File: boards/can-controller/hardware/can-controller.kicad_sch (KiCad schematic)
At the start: 1 part, among them J1 RPi_GPIO

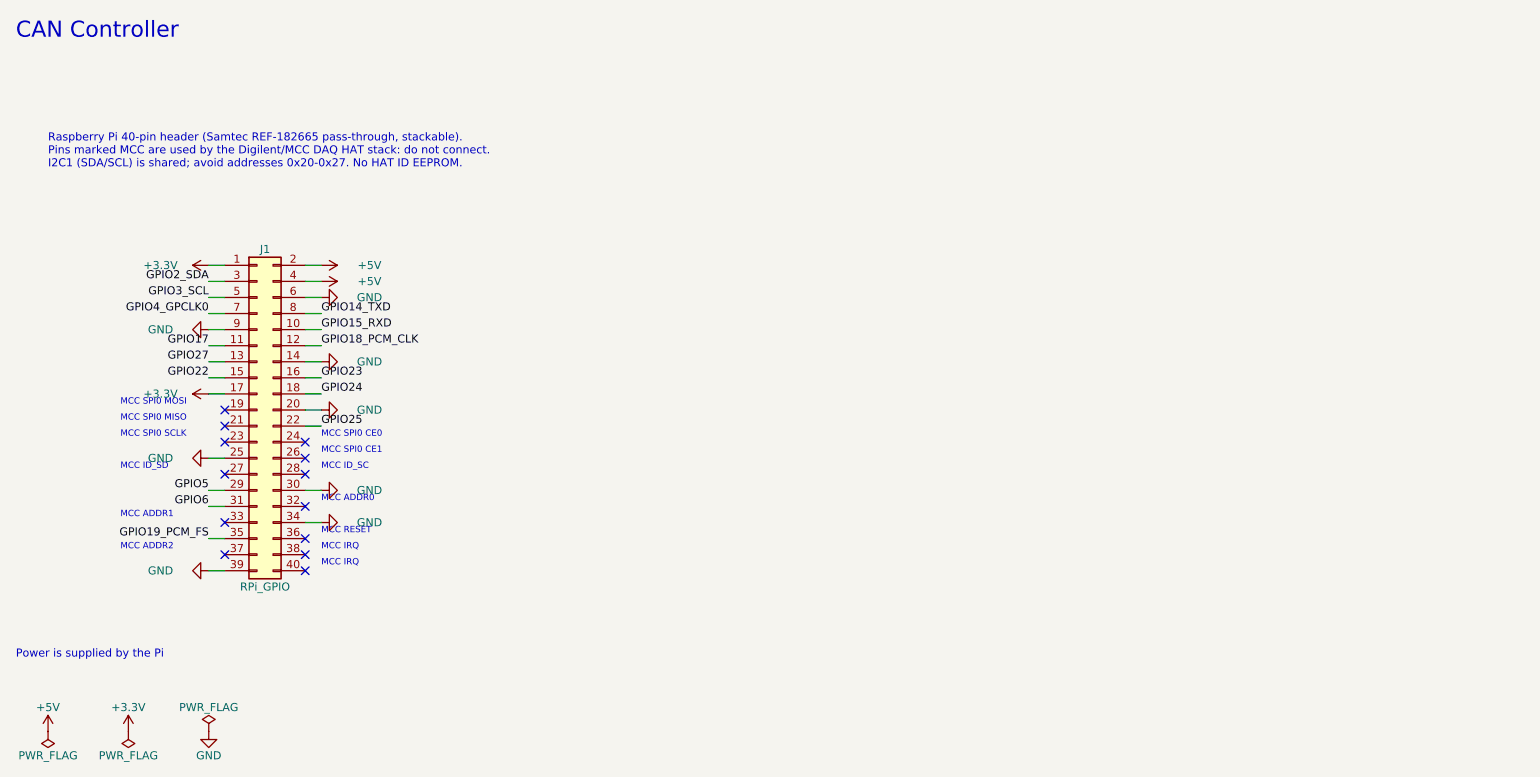
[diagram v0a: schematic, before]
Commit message: can-controller: first schematic capture (7 sheets), footprints parked
- gen_schematic.py (first capture only, like can-ssr's): MCU/USB/power,
  CAN x4 (ISO1044BD; +12 V fuse fitted on CAN1, DNP on CAN2-4), 12 V input
  (NANO2 fuse, SUD50P04-08 reverse-polarity P-FET, SMBJ15A, R-78E 5 V for
  the bus sides, TLP293 12 V status), relay drive (2 x ISO6740, ULN2803A,
  logic-side LEDs), GPIO (8 x 4.7k + BAT54S), analog in (MCP3428, dividers
  referenced to VMID because the ADC cannot go below VSS), analog out
  (MCP4922 + LM4040 2.5 V, LM358B gain 4 on a 13 V TPS61040 boost,
  470R + 15 V Zener output protection)
- MCU pin map checked against the PPS group tables of DS60001519E
- ERC 0, parity clean; only isolators span the two domains
- PCB: footprints synced and parked; template copper removed
- sync_pcb.py now carries the DNP attribute to the PCB
- House DRC rule: 0.15 mm annular ring for the GCT USB4085 only
- 3D models for SOIC-4 (SOP-4) and the 1812 PTC (C_1812 stand-in)

Co-Authored-By: Claude Opus 5.5 <noreply@anthropic.com>
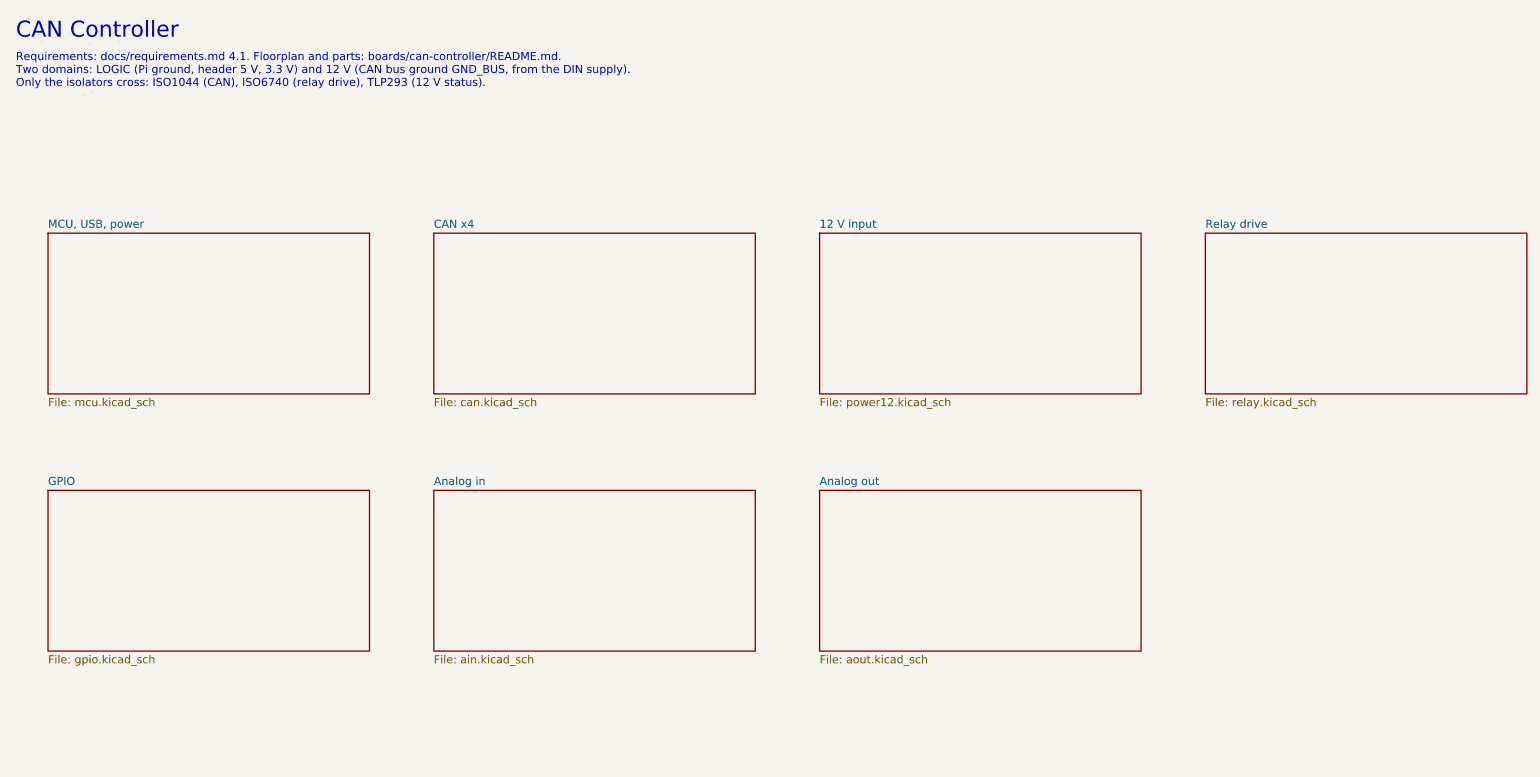
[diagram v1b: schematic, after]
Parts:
- removed J1: RPi_GPIO, Thl_Connector:Samtec_REF-182665_2x20_P2.54mm_PassThrough, symbol Connector_Generic:Conn_02x20_Odd_Even
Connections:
- no-connect marks 13 -> 0
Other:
- added sheet 12 V input (power12.kicad_sch)
- added sheet Analog in (ain.kicad_sch)
- added sheet Analog out (aout.kicad_sch)
- added sheet CAN x4 (can.kicad_sch)
- added sheet GPIO (gpio.kicad_sch)
- added sheet MCU, USB, power (mcu.kicad_sch)
- added sheet Relay drive (relay.kicad_sch)
- note added: "Requirements: docs/requirements.md 4.1. Floorplan and parts: boards/can-controller/README.md. Two domains: LOGIC (Pi ground, header 5 V, 3.3 V) and 12 V (CAN bus ground GND_BUS, from the DIN supply). Only the isolators cross: ISO1044 (CAN), ISO6740 (relay drive), TLP293 (12 V status)."
- note removed: "MCC ADDR0"
- note removed: "MCC ADDR1"
- note removed: "MCC ADDR2"
- note removed: "MCC ID_SC"
- note removed: "MCC ID_SD"
- note removed: "MCC IRQ"
- note removed: "MCC RESET"
- note removed: "MCC SPI0 CE0"
- note removed: "MCC SPI0 CE1"
- note removed: "MCC SPI0 MISO"
- note removed: "MCC SPI0 MOSI"
- note removed: "MCC SPI0 SCLK"
- note removed: "Power is supplied by the Pi"
- note removed: "Raspberry Pi 40-pin header (Samtec REF-182665 pass-through, stackable). Pins marked MCC are used by the Digilent/MCC DAQ HAT stack: do not connect. I2C1 (SDA/SCL) is shared; avoid addresses 0x20-0x27. No HAT ID EEPROM."

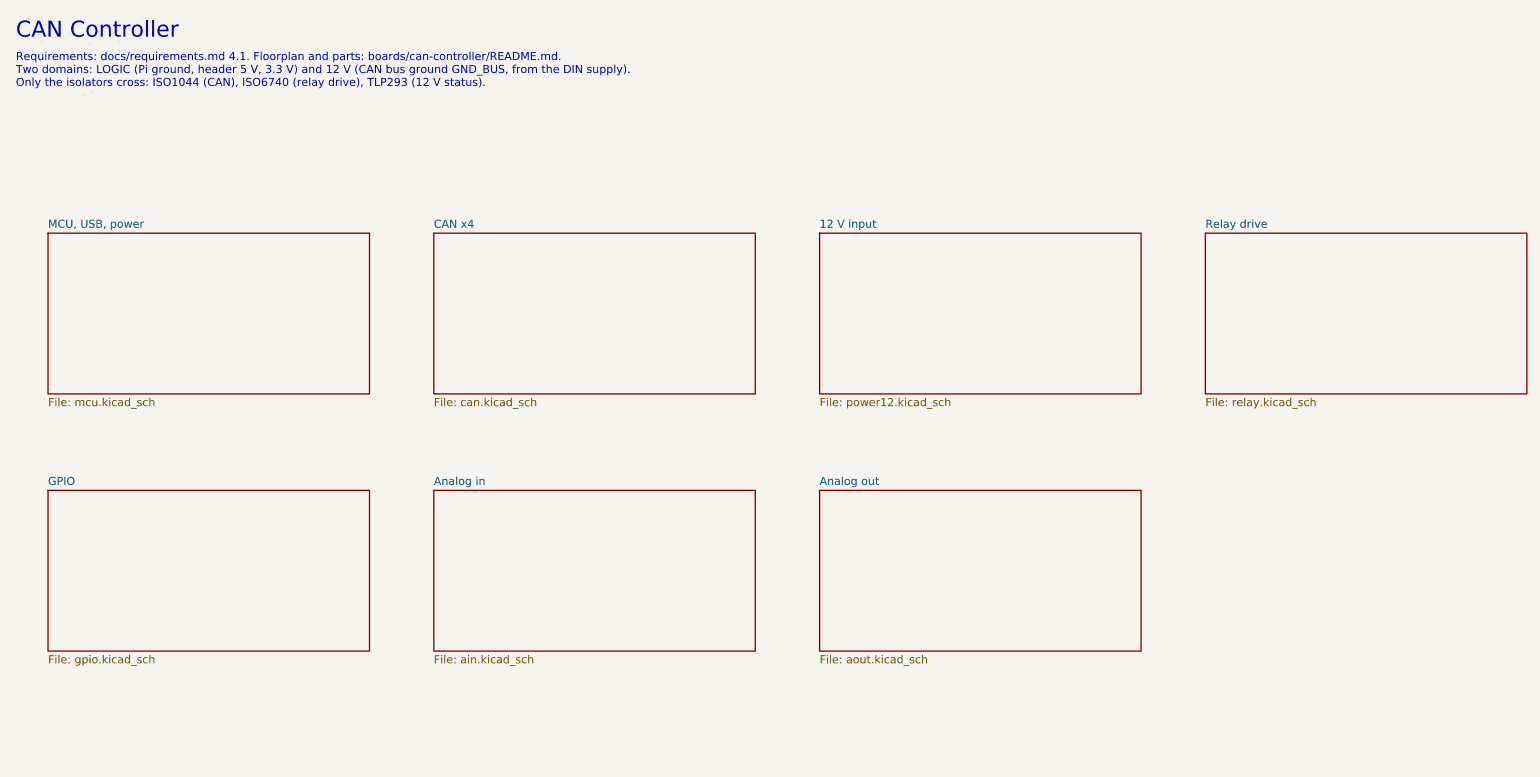
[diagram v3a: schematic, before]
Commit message: can-controller: schematic for the new scope (Ethernet W6100, 4 x ISOW1044, AQW212 relays, diff AI)
Six sheets generated by gen_schematic.py: MCU and logic power, Ethernet,
CAN x4, 12 V input and isolated logic supply (TDN 5-2411WI), relay drive,
GPIO and analog in. ERC 0; netlist check: no net crosses a domain except
at the designed crossings. New lib parts: Thl_Interface:W6100-L (flat),
Thl_Isolator:AQW212, stock ISOW1044 / TDN 5WI / LQFP-48 / bead footprints.
PCB still holds the old layout (next: update from schematic, placement).

Co-Authored-By: Claude Opus 5.5 <noreply@anthropic.com>
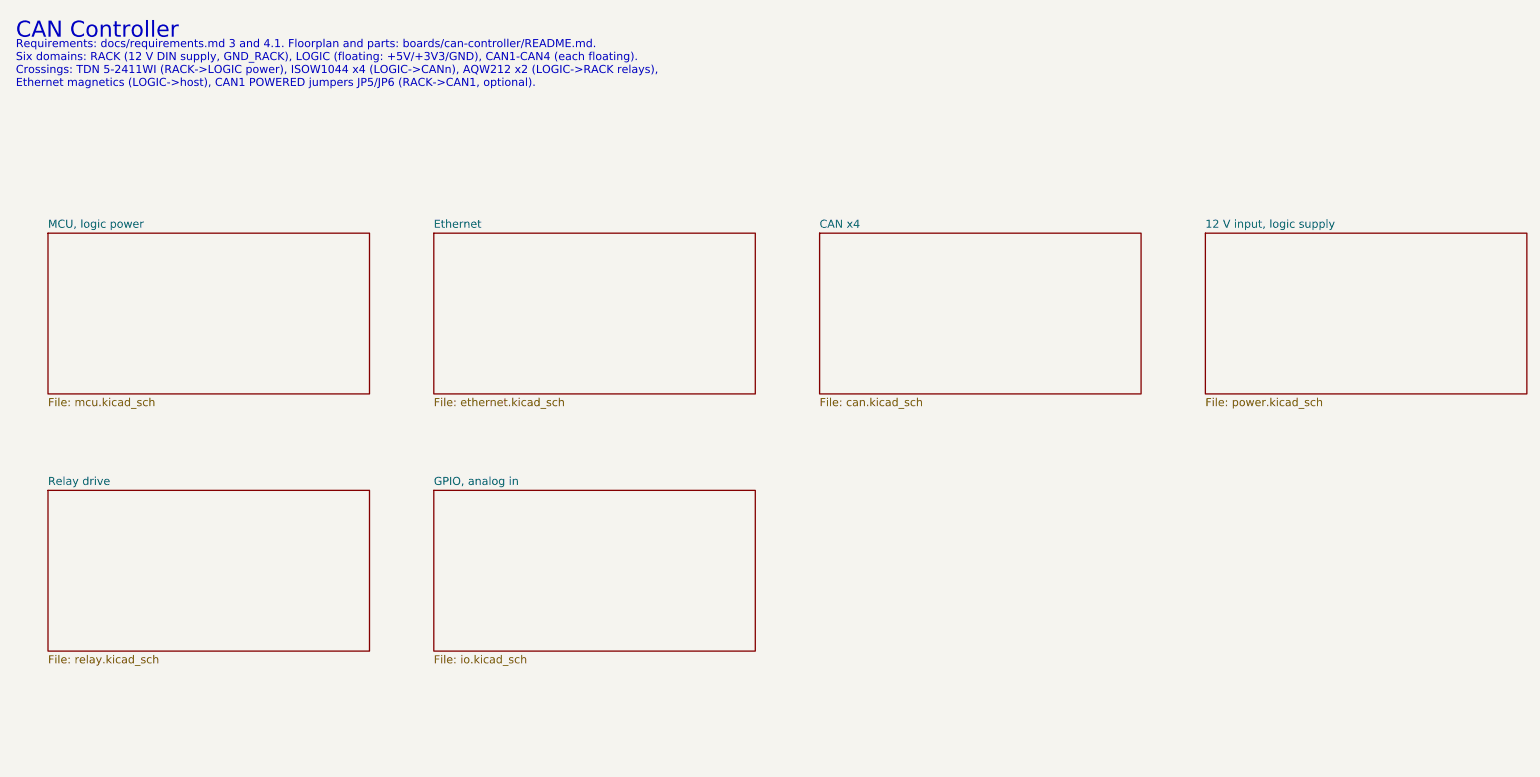
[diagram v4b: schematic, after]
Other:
- removed sheet 12 V input
- removed sheet Analog in
- removed sheet Analog out
- removed sheet GPIO
- removed sheet MCU, USB, power
- added sheet 12 V input, logic supply (power.kicad_sch)
- added sheet Ethernet (ethernet.kicad_sch)
- added sheet GPIO, analog in (io.kicad_sch)
- added sheet MCU, logic power (mcu.kicad_sch)
- note added: "Requirements: docs/requirements.md 3 and 4.1. Floorplan and parts: boards/can-controller/README.md. Six domains: RACK (12 V DIN supply, GND_RACK), LOGIC (floating: +5V/+3V3/GND), CAN1-CAN4 (each floating). Crossings: TDN 5-2411WI (RACK->LOGIC power), ISOW1044 x4 (LOGIC->CANn), AQW212 x2 (LOGIC->RACK relays), Ethernet magnetics (LOGIC->host), CAN1 POWERED jumpers JP5/JP6 (RACK->CAN1, optional)."
- note removed: "Requirements: docs/requirements.md 4.1. Floorplan and parts: boards/can-controller/README.md. Two domains: LOGIC (Pi ground, header 5 V, 3.3 V) and 12 V (CAN bus ground GND_BUS, from the DIN supply). Only the isolators cross: ISO1044 (CAN), ISO6740 (relay drive), TLP293 (12 V status)."
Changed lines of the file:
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@@
 	(title_block
 		(title "CAN Controller")
-		(date "2026-10-05")
+		(date "2026-10-06")
 		(rev "A")
 	)
@@
 		)
 	)
-	(text "Requirements: docs/requirements.md 4.1. Floorplan and parts: boards/can-controller/README.md.\nTwo domains: LOGIC (Pi ground, header 5 V, 3.3 V) and 12 V (CAN bus ground GND_BUS, from the DIN supply).\nOnly the isolators cross: ISO1044 (CAN), ISO6740 (relay drive), TLP293 (12 V status)."
+	(text "Requirements: docs/requirements.md 3 and 4.1. Floorplan and parts: boards/can-controller/README.md.\nSix domains: RACK (12 V DIN supply, GND_RACK), LOGIC (floating: +5V/+3V3/GND), CAN1-CAN4 (each floating).\nCrossings: TDN 5-2411WI (RACK->LOGIC power), ISOW1044 x4 (LOGIC->CANn), AQW212 x2 (LOGIC->RACK relays),\nEthernet magnetics (LOGIC->host), CAN1 POWERED jumpers JP5/JP6 (RACK->CAN1, optional)."
 		(exclude_from_sim no)
 		(at 25.4 38.1 0)
@@
 			(color 0 0 0 0.0000)
 		)
-		(property "Sheetname" "MCU, USB, power"
+		(property "Sheetname" "MCU, logic power"
 			(at 30.48 60.26 0)
 			(effects
@@
 			(color 0 0 0 0.0000)
 		)
+		(property "Sheetname" "Ethernet"
+			(at 91.44 60.26 0)
+			(effects
+				(font
+					(size 1.27 1.27)
+				)
+				(justify left bottom)
+			)
+		)
+		(property "Sheetfile" "ethernet.kicad_sch"
+			(at 91.44 86.96 0)
+			(effects
+				(font
+					(size 1.27 1.27)
+				)
+				(justify left top)
+			)
+		)
+		(instances
+			(project "can-controller"
+				(path "/3b432fe7-d4c7-43d1-9eb2-554f75f608a8"
+					(page "3")
+				)
+			)
+		)
+	)
+	(sheet
+		(at 152.4 60.96)
+		(size 50.8 25.4)
+		(exclude_from_sim no)
+		(in_bom yes)
+		(on_board yes)
+		(dnp no)
+		(fields_autoplaced yes)
+		(stroke
+			(width 0.1524)
+			(type solid)
+		)
+		(fill
+			(color 0 0 0 0.0000)
+		)
 		(property "Sheetname" "CAN x4"
-			(at 91.44 60.26 0)
+			(at 152.4 60.26 0)
 			(effects
 				(font
@@
 		)
 		(property "Sheetfile" "can.kicad_sch"
-			(at 91.44 86.96 0)
-			(effects
-				(font
-					(size 1.27 1.27)
-				)
-				(justify left top)
-			)
-		)
-		(instances
-			(project "can-controller"
-				(path "/3b432fe7-d4c7-43d1-9eb2-554f75f608a8"
-					(page "3")
-				)
-			)
-		)
-	)
-	(sheet
-		(at 152.4 60.96)
-		(size 50.8 25.4)
-		(exclude_from_sim no)
-		(in_bom yes)
-		(on_board yes)
-		(dnp no)
-		(fields_autoplaced yes)
-		(stroke
-			(width 0.1524)
-			(type solid)
-		)
-		(fill
-			(color 0 0 0 0.0000)
-		)
-		(property "Sheetname" "12 V input"
-			(at 152.4 60.26 0)
-			(effects
-				(font
-					(size 1.27 1.27)
-				)
-				(justify left bottom)
-			)
-		)
-		(property "Sheetfile" "power12.kicad_sch"
 			(at 152.4 86.96 0)
 			(effects
@@
 			(color 0 0 0 0.0000)
 		)
+		(property "Sheetname" "12 V input, logic supply"
+			(at 213.36 60.26 0)
+			(effects
+				(font
+					(size 1.27 1.27)
+				)
+				(justify left bottom)
+			)
+		)
+		(property "Sheetfile" "power.kicad_sch"
+			(at 213.36 86.96 0)
+			(effects
+				(font
+					(size 1.27 1.27)
+				)
+				(justify left top)
+			)
+		)
+		(instances
+			(project "can-controller"
+				(path "/3b432fe7-d4c7-43d1-9eb2-554f75f608a8"
+					(page "5")
+				)
+			)
+		)
+	)
+	(sheet
+		(at 30.48 101.6)
+		(size 50.8 25.4)
+		(exclude_from_sim no)
+		(in_bom yes)
+		(on_board yes)
+		(dnp no)
+		(fields_autoplaced yes)
+		(stroke
+			(width 0.1524)
+			(type solid)
+		)
+		(fill
+			(color 0 0 0 0.0000)
+		)
 		(property "Sheetname" "Relay drive"
-			(at 213.36 60.26 0)
+			(at 30.48 100.9 0)
 			(effects
 				(font
@@
 		)
 		(property "Sheetfile" "relay.kicad_sch"
-			(at 213.36 86.96 0)
-			(effects
-				(font
-					(size 1.27 1.27)
-				)
-				(justify left top)
-			)
-		)
-		(instances
-			(project "can-controller"
-				(path "/3b432fe7-d4c7-43d1-9eb2-554f75f608a8"
-					(page "5")
-				)
-			)
-		)
-	)
-	(sheet
-		(at 30.48 101.6)
-		(size 50.8 25.4)
-		(exclude_from_sim no)
-		(in_bom yes)
-		(on_board yes)
-		(dnp no)
-		(fields_autoplaced yes)
-		(stroke
-			(width 0.1524)
-			(type solid)
-		)
-		(fill
-			(color 0 0 0 0.0000)
-		)
-		(property "Sheetname" "GPIO"
-			(at 30.48 100.9 0)
-			(effects
-				(font
-					(size 1.27 1.27)
-				)
-				(justify left bottom)
-			)
-		)
-		(property "Sheetfile" "gpio.kicad_sch"
 			(at 30.48 127.6 0)
 			(effects
@@
 			(color 0 0 0 0.0000)
 		)
-		(property "Sheetname" "Analog in"
+		(property "Sheetname" "GPIO, analog in"
 			(at 91.44 100.9 0)
 			(effects
@@
 			)
 		)
-		(property "Sheetfile" "ain.kicad_sch"
+		(property "Sheetfile" "io.kicad_sch"
 			(at 91.44 127.6 0)
 			(effects
@@
 				)
 			)
-		)
-	)
-	(sheet
-		(at 152.4 101.6)
-		(size 50.8 25.4)
-		(exclude_from_sim no)
-		(in_bom yes)
-		(on_board yes)
-		(dnp no)
-		(fields_autoplaced yes)
-		(stroke
-			(width 0.1524)
-			(type solid)
-		)
-		(fill
-			(color 0 0 0 0.0000)
-		)
-		(property "Sheetname" "Analog out"
-			(at 152.4 100.9 0)
-			(effects
-				(font
-					(size 1.27 1.27)
-				)
-				(justify left bottom)
-			)
-		)
-		(property "Sheetfile" "aout.kicad_sch"
-			(at 152.4 127.6 0)
-			(effects
-				(font
-					(size 1.27 1.27)
-				)
-				(justify left top)
-			)
-		)
-		(instances
-			(project "can-controller"
-				(path "/3b432fe7-d4c7-43d1-9eb2-554f75f608a8"
-					(page "8")
-				)
-			)
